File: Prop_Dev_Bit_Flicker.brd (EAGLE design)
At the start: 63.2 x 24.9 mm, 67 parts, among them J1 MF-CON-MICROUSB-RIGHT, J4 M20-7822046, J5 M20-7822046, U1 P8X32A-Q44, U2 FT230XQ-R, U3 TPS2113ADRBR, U4 CAT24C512WI-GT3, U5 MAX11613EUA+, U6 NCP1117LPST33T3G, U7 IRLML6401TRPBF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

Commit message: Working on layout.
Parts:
- moved C10 46.2 mm to (6.86, 39.1)
- moved C18 45.1 mm to (7.37, 8.76), turned to 0 degrees
- moved U$1 42.3 mm to (73.4, 25.7)
- moved C19 42.1 mm to (7.37, 13.3), turned to 0 degrees
- moved C9 38.8 mm to (8.89, 34.5)
- moved C11 38.2 mm to (11.7, 40.1)
- moved C8 37.6 mm to (19.3, 40.6)
- moved L2 36.1 mm to (1.91, 19.4)
- moved U6 35.2 mm to (17.8, 34.3)
- moved U8 26.8 mm to (57.1, 12.4), flipped to the bottom, turned to 90 degrees
- moved C14 21.6 mm to (82.0, 3.81)
- moved U5 19.7 mm to (80.8, 10.2)
- moved U4 4.33 mm to (24.9, 12.4)
- moved R4 4.06 mm to (18.0, 11.7)
- moved R5 4.06 mm to (18.0, 10.2)
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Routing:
- net N$3: track 0.00 -> 15.1 mm
- net GND: track 0.00 -> 6.39 mm, vias 0 -> 4
- net D+: track 0.00 -> 5.66 mm
- net N$41: track 0.00 -> 4.52 mm, vias 0 -> 1
- net D-: track 0.00 -> 4.07 mm
- net VBUS_P1: track 0.00 -> 3.82 mm
- net USBDP: track 0.00 -> 3.73 mm, vias 0 -> 1
- net VBUS: track 0.00 -> 3.15 mm
- net USBDM: track 0.00 -> 2.93 mm, vias 0 -> 1
- net N$1: track 0.00 -> 1.96 mm
- net N$2: track 0.00 -> 1.91 mm
- added copper zone on layer 15, net 3.3V
- added copper zone on layer 2, net GND
- removed copper zone on layer 16, net 3.3V
- removed copper zone on layer 1, net GND
- removed copper zone on layer 16, net GND

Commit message: Working on layout.
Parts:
- moved C11 44.3 mm to (39.4, 5.59), turned to 270 degrees
- moved C10 42.4 mm to (32.8, 5.59), turned to 270 degrees
- moved C9 40.6 mm to (37.3, 5.59), turned to 270 degrees
- moved C8 38.3 mm to (34.8, 5.59), turned to 90 degrees
- moved U6 29.3 mm to (37.1, 12.2), turned to 0 degrees
- moved C6 1.61 mm to (29.5, 5.59)
- moved C15 1.61 mm to (12.7, 18.8), turned to 0 degrees
- moved C4 1.52 mm to (36.3, 12.2)
- moved C5 1.17 mm to (20.6, 12.2)
- moved U1 0.57 mm to (28.7, 12.2)
- moved C7 0.38 mm to (15.2, 8.00)
- moved R14 0.25 mm to (16.1, 5.59)
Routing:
- net GND: track 6.39 -> 123.8 mm, vias 4 -> 22
- net 3.3V: track 0.00 -> 61.5 mm, vias 0 -> 12
- net VIN: track 0.00 -> 47.6 mm, vias 0 -> 2
- net VBUS_P2: track 0.00 -> 44.1 mm, vias 0 -> 2
- net RX: track 0.00 -> 42.4 mm, vias 0 -> 2
- net SDA: track 0.00 -> 37.4 mm
- net SD_CS: track 0.00 -> 34.4 mm
- net SD_DI: track 0.00 -> 31.0 mm
- net SCL: track 0.00 -> 28.3 mm, vias 0 -> 1
- net SD_SCLK: track 0.00 -> 28.3 mm
- net TX: track 0.00 -> 27.9 mm, vias 0 -> 1
- net SD_DO: track 0.00 -> 26.4 mm
- net RES: track 0.00 -> 23.7 mm, vias 0 -> 2
- net P15: track 0.00 -> 23.0 mm
- net P16: track 0.00 -> 22.9 mm
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
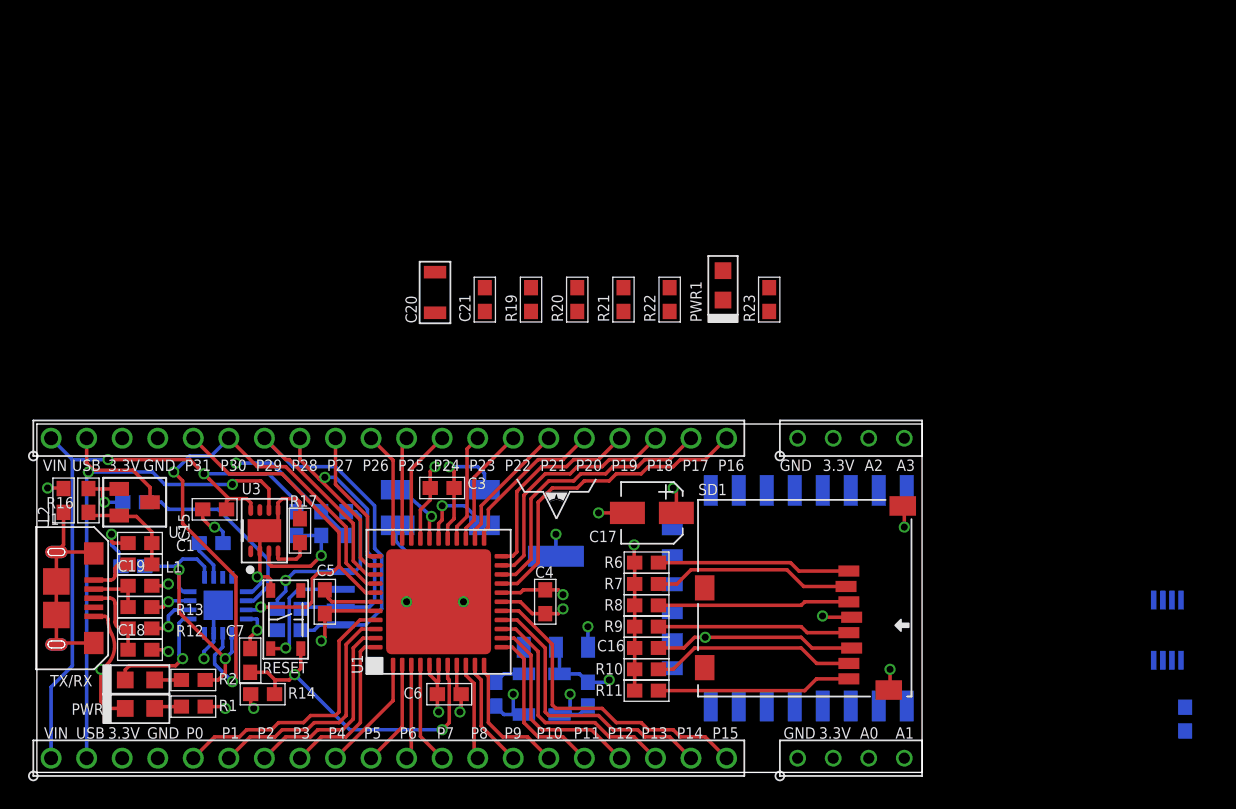
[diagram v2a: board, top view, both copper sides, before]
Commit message: preliminary layout complete.
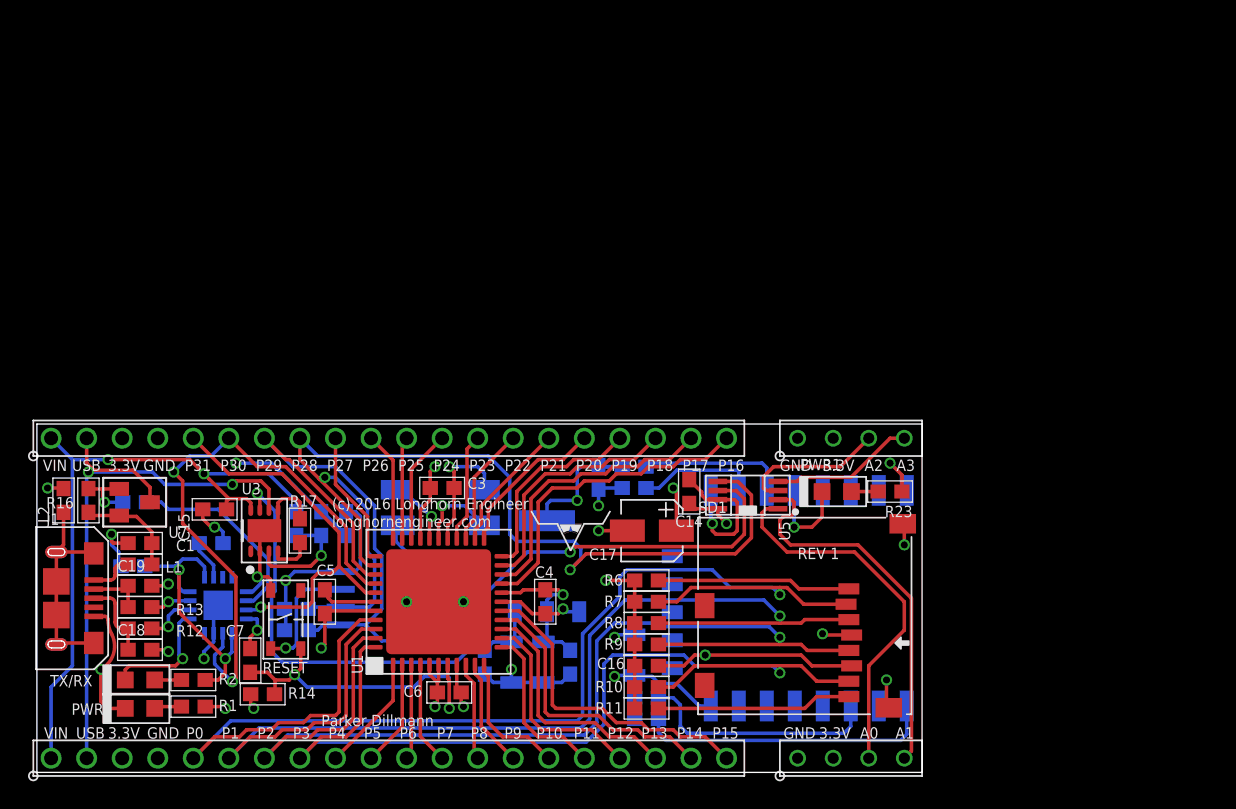
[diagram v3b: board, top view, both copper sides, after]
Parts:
- moved U$1 53.7 mm to (21.1, 13.7), flipped to the top
- moved C14 39.0 mm to (46.6, 20.1), flipped to the top
- moved U5 31.5 mm to (50.8, 19.8), flipped to the top, turned to 180 degrees
- moved R22 30.0 mm to (43.6, 3.81), flipped to the bottom, turned to 180 degrees
- moved C20 29.6 mm to (42.7, 8.38), flipped to the bottom
- moved R20 28.9 mm to (43.6, 5.33), flipped to the bottom, turned to 180 degrees
- moved PWR1 16.8 mm to (57.1, 20.1), turned to 0 degrees
- moved R23 16.2 mm to (61.0, 20.1), turned to 180 degrees
- moved C21 15.1 mm to (40.1, 21.1), flipped to the bottom, turned to 270 degrees
- moved R19 14.0 mm to (42.7, 21.8), flipped to the bottom, turned to 180 degrees
- moved R21 13.5 mm to (42.7, 20.3), flipped to the bottom, turned to 0 degrees
- moved U6 2.62 mm to (36.4, 14.7)
- moved C11 2.62 mm to (38.1, 7.87)
- moved C9 2.56 mm to (36.2, 7.87)
- moved U$2 2.50 mm to (40.1, 15.7)
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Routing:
- net SD_CS: track 34.4 -> 87.4 mm, vias 0 -> 1
- net SD_DI: track 31.0 -> 79.5 mm, vias 0 -> 1
- net SCL: track 28.3 -> 75.9 mm, vias 1 -> 2
- net SD_SCLK: track 28.3 -> 73.4 mm, vias 0 -> 1
- net SD_DO: track 26.4 -> 67.3 mm, vias 0 -> 1
- net SDA: track 37.4 -> 73.1 mm, vias 0 -> 1
- net 3.3V: track 61.5 -> 91.5 mm, vias 12 -> 14
- net 5V: track 4.19 -> 33.6 mm, vias 0 -> 1
- net A1: track 0.00 -> 27.2 mm
- net A0: track 0.00 -> 26.9 mm
- net WIFI_RST: track 0.00 -> 21.2 mm
- net CH_PD: track 0.00 -> 17.3 mm
- net GND: track 123.8 -> 139.8 mm, vias 22 -> 23
- net A2: track 0.00 -> 10.6 mm
- net GPIO2: track 0.00 -> 10.5 mm
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
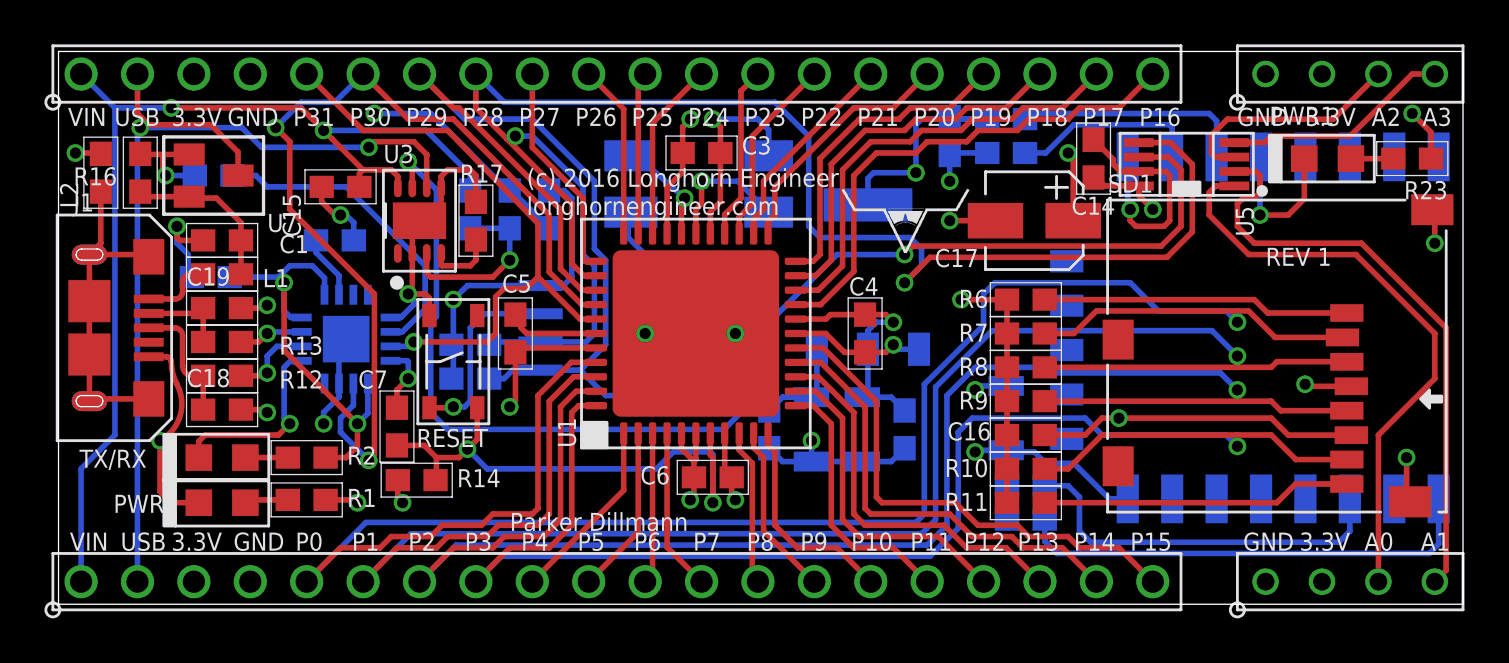
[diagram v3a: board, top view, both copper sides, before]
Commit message: top done. bottom next on silkscreen and trace clean u
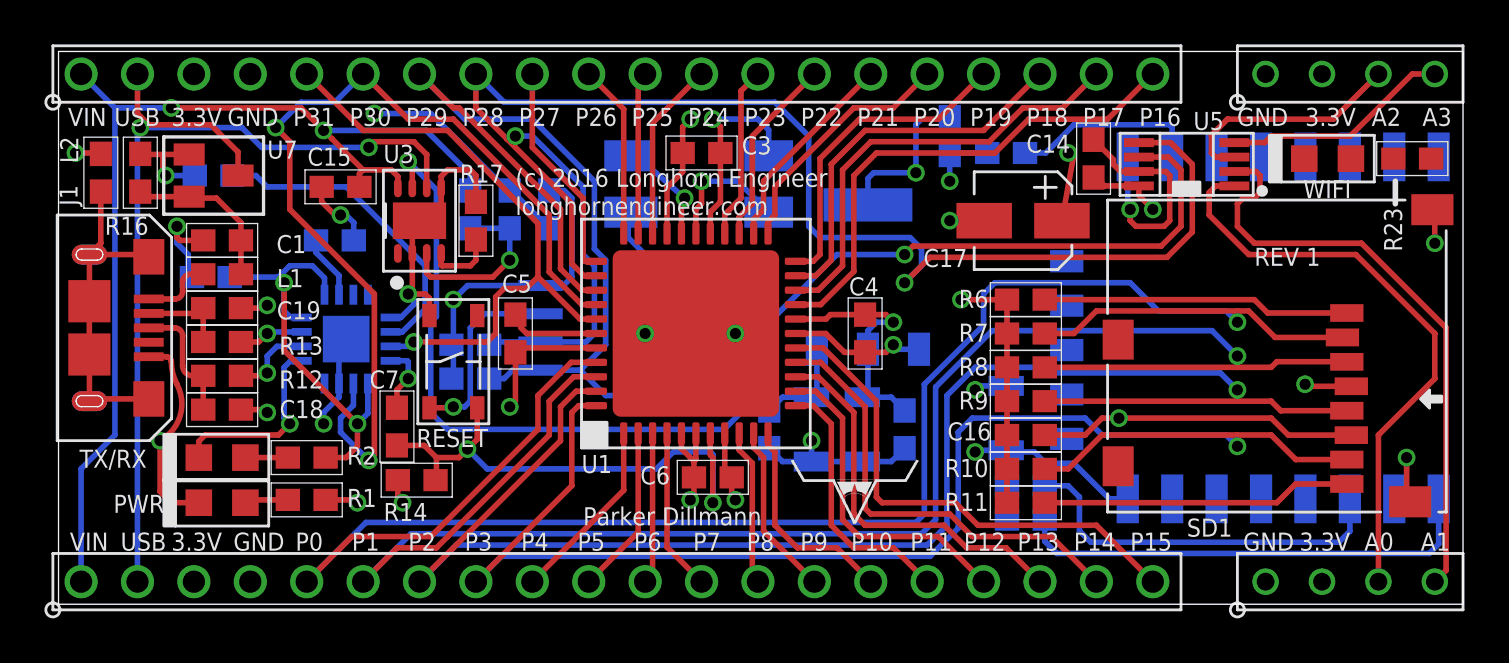
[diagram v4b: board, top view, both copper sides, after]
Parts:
- removed R19: 10K, PP_Passives:0603
- moved U$2 12.4 mm to (37.8, 3.56)
- moved U8 1.91 mm to (55.2, 12.4)
- moved C17 0.51 mm to (43.4, 17.3)
- moved U$1 0.51 mm to (20.6, 13.7)
- renumbered PWR1 to WIFI
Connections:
- removed net GPIO2: R19.2, U8.P$17
- removed net N$4: R23.2, WIFI.ANODE
- removed net N$9: U8.P$18, WIFI.CATHODE
- net 3.3V: no longer R19.1, R23.1
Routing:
- net GPIO2: track 10.5 -> 0.00 mm
- net 3.3V: track 91.5 -> 84.1 mm, vias 14 -> 13
- net N$9: track 6.75 -> 0.00 mm, vias 1 -> 0
- net SD_DI: track 79.5 -> 77.4 mm
- net SD_CS: track 87.4 -> 85.3 mm
- net SD_SCLK: track 73.4 -> 71.4 mm
- net N$4: track 1.91 -> 0.00 mm
- net SD_DO: track 67.3 -> 66.2 mm
- net GND: track 139.8 -> 139.3 mm

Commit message: Finished REV 2. Added Fids.
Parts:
- removed R23: 1K, PP_Passives:0603
- removed WIFI: 598-8020-107F, PP_LED:LED_0805
- added FID1, FID2, FID3, FID4: FIDUCIAL_0.5MM, MF_Aesthetics:FIDUCIAL_0.5MM
- moved U$1 24.4 mm to (-1.02, 2.29), flipped to the bottom, turned to 90 degrees
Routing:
- net VBUS_P1: track 10.3 -> 14.0 mm, vias 0 -> 1
- net GND: track 139.3 -> 142.3 mm, vias 23 -> 24
- net 3.3V: track 84.1 -> 85.4 mm
- added copper zone on layer 16, net 3.3V

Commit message: Added DB
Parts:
- added U$3: DB_LOGO_SILK_SMALL, PP_Aesthetics:DB_SILK_SMALL
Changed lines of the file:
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@@
 <element name="FID3" library="MF_Aesthetics" package="FIDUCIAL_0.5MM" value="FIDUCIAL_0.5MM" x="2.286" y="4.826" rot="MR0"/>
 <element name="FID4" library="MF_Aesthetics" package="FIDUCIAL_0.5MM" value="FIDUCIAL_0.5MM" x="51.816" y="23.622" rot="MR0"/>
+<element name="U$3" library="PP_Aesthetics" package="DB_SILK_SMALL" value="DB_LOGO_SILK_SMALL" x="49.53" y="10.922"/>
 </elements>
 <signals>

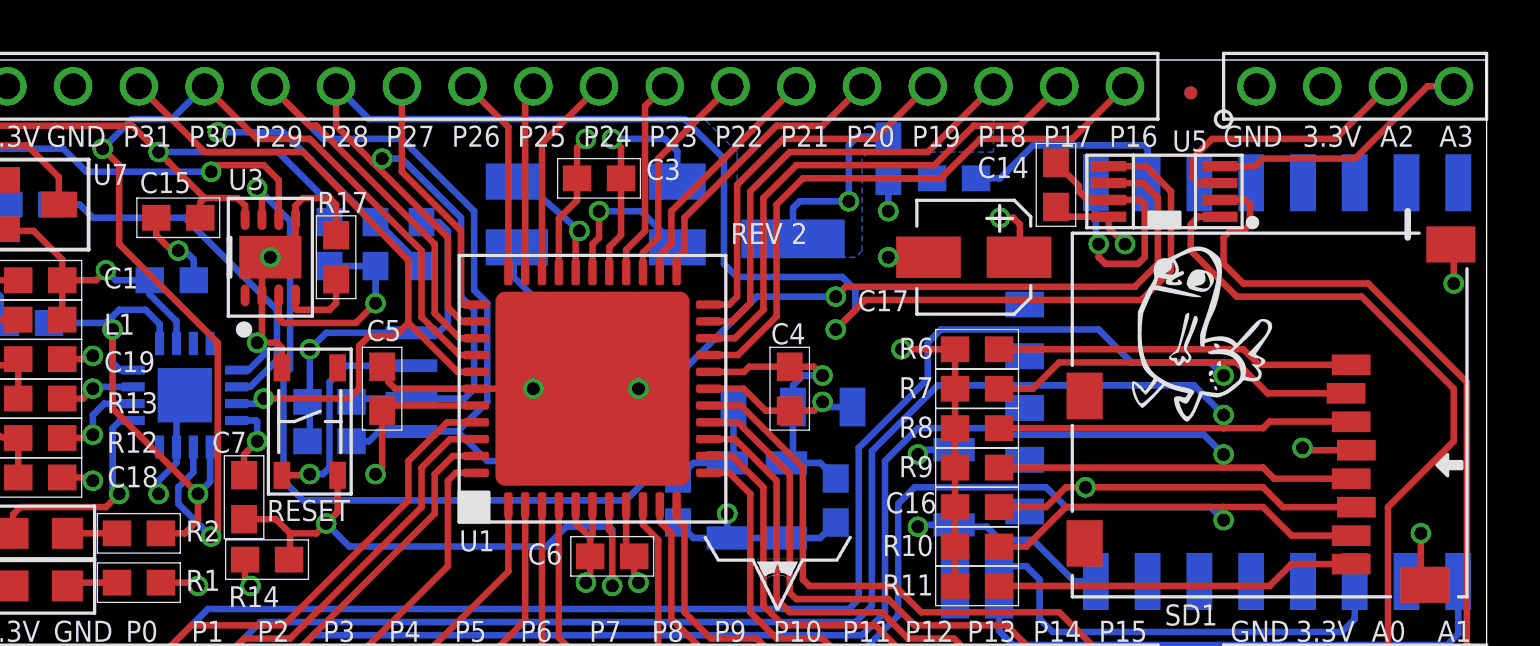
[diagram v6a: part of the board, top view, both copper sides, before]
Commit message: Switch added to GPIO0 for the ESP-12E for flashing.
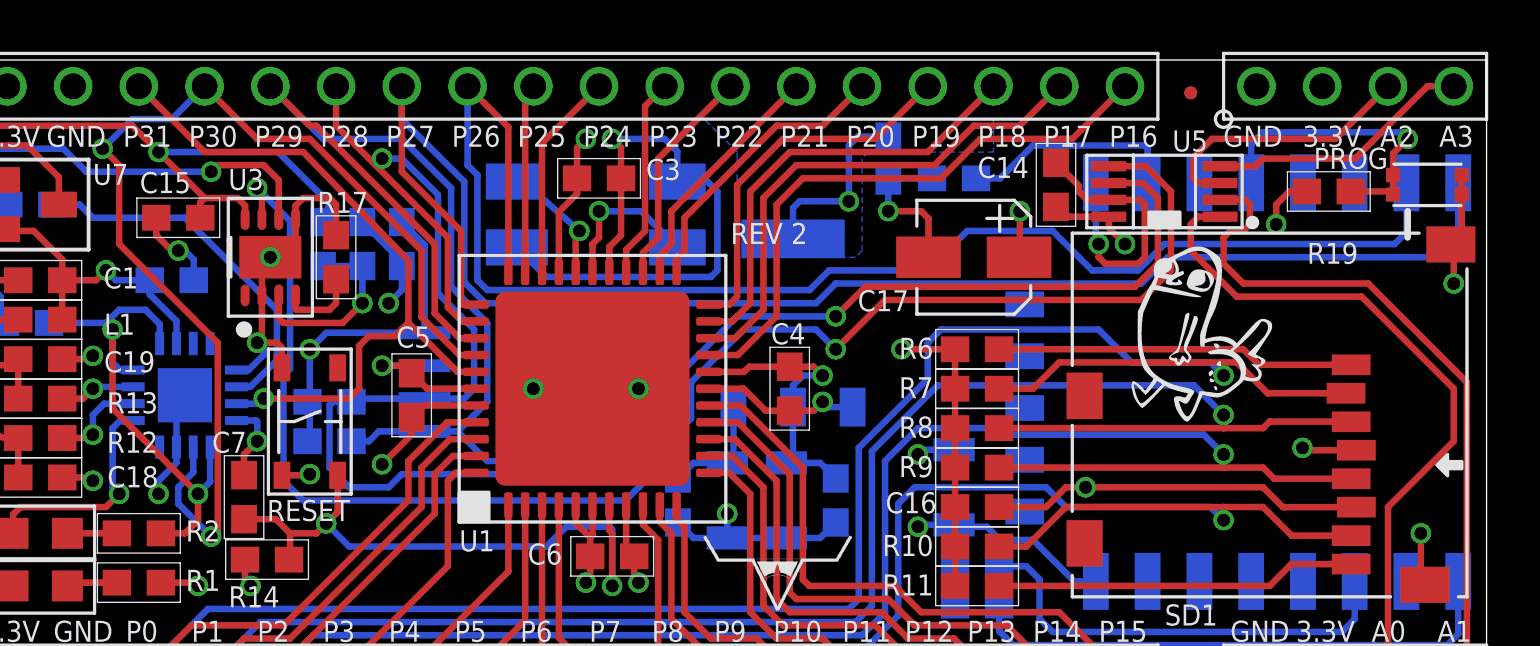
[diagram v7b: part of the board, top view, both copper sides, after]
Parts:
- added PROG: EVP-BB2A1B000, PP_Electromechanical:EVPBB
- added R19: 10K, PP_Passives:0603
- moved C5 1.17 mm to (21.7, 11.9)
- moved C12 0.76 mm to (21.3, 17.8)
- moved R18 0.51 mm to (19.8, 17.8)
- moved U4 0.51 mm to (25.4, 12.4)
- moved R3 0.25 mm to (18.3, 17.8)
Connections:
- removed net P26: J5.10, U1.33
- removed net P27: J5.9, U1.34
- new net GPIO0: PROG.P$1, PROG.P$2, R19.2, U8.P$18
- net 3.3V: now also R19.1
- net GND: now also PROG.P$3, PROG.P$4
- net WIFI_RX: now also J5.10, U1.33
- net WIFI_TX: now also J5.9, U1.34
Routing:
- net WIFI_TX: track 0.00 -> 60.4 mm
- net WIFI_RX: track 0.00 -> 55.6 mm
- net GPIO0: track 0.00 -> 11.9 mm, vias 0 -> 1
- net P27: track 9.93 -> 0.00 mm
- net P26: track 7.84 -> 0.00 mm
- net GND: track 142.3 -> 141.1 mm
- net VSNS: track 8.23 -> 7.46 mm
- net 3.3V: track 85.4 -> 85.1 mm, vias 13 -> 14
